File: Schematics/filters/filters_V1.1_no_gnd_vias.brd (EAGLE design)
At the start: 100.6 x 47.9 mm, 110 parts, among them IC1 NE5532N, IC2 NE5532N, IC3 NE5532N, IC4 NE5532N, IC5 NE5532N, IC6 NE5532N, IC7 NE5532N, J1 3_PIN_AMPCONN, J2 3_PIN_AMPCONN, J3 3_PIN_AMPCONN

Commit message: newest gerbers
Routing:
- net N$5: vias 1 -> 0
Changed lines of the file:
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@@
 <wire x1="12.7" y1="15.5575" x2="12.7" y2="14.605" width="0.4064" layer="16"/>
 <wire x1="12.7" y1="14.605" x2="14.605" y2="12.7" width="0.4064" layer="16"/>
-<via x="14.605" y="12.7" extent="1-16" drill="0.381"/>
+<wire x1="14.605" y1="12.7" x2="14.605" y2="12.7" width="0" layer="19" extent="1-16"/>
 <wire x1="14.605" y1="12.7" x2="16.8275" y2="10.4775" width="0.4064" layer="1"/>
 <wire x1="16.8275" y1="10.4775" x2="16.8275" y2="8.4826125" width="0.4064" layer="1"/>
@@
 <contactref element="L12" pad="2"/>
 <contactref element="C11" pad="1"/>
-<via x="32.7025" y="30.1625" extent="1-16" drill="0.8128"/>
+<via x="32.7025" y="30.1625" extent="1-16" drill="0.508"/>
 <wire x1="32.7025" y1="30.1625" x2="32.7025" y2="35.56" width="0.4064" layer="1"/>
 <wire x1="35.56" y1="36.195" x2="37.505" y2="36.195" width="0.8128" layer="1"/>
@@
 <contactref element="R29" pad="2"/>
 <contactref element="VR4" pad="1'"/>
-<via x="80.5815" y="5.08" extent="1-16" drill="0.8128"/>
+<via x="80.5815" y="5.08" extent="1-16" drill="0.508"/>
 <wire x1="80.5815" y1="5.08" x2="74.6125" y2="5.08" width="0.4064" layer="16"/>
 <wire x1="74.6125" y1="5.08" x2="73.9775" y2="4.445" width="0.4064" layer="16"/>
@@
 <contactref element="VR3" pad="1'"/>
 <wire x1="58.1025" y1="7.62" x2="58.1025" y2="5.08" width="0.4064" layer="1"/>
-<via x="58.1025" y="5.08" extent="1-16" drill="0.8128"/>
+<via x="58.1025" y="5.08" extent="1-16" drill="0.508"/>
 <wire x1="58.1025" y1="5.08" x2="52.07" y2="5.08" width="0.4064" layer="16"/>
 <wire x1="52.07" y1="5.08" x2="51.435" y2="4.445" width="0.4064" layer="16"/>
@@
 <contactref element="VR2" pad="1'"/>
 <wire x1="35.56" y1="6.985" x2="35.56" y2="5.3975" width="0.4064" layer="1"/>
-<via x="35.56" y="5.3975" extent="1-16" drill="0.8128"/>
+<via x="35.56" y="5.3975" extent="1-16" drill="0.508"/>
 <wire x1="35.56" y1="5.3975" x2="29.21" y2="5.3975" width="0.4064" layer="16"/>
 <wire x1="29.21" y1="5.3975" x2="28.575" y2="4.7625" width="0.4064" layer="16"/>
@@
 <wire x1="96.2025" y1="7.9375" x2="90.805" y2="7.9375" width="0.4064" layer="1"/>
 <wire x1="90.805" y1="7.9375" x2="90.805" y2="10.4775" width="0.4064" layer="1"/>
-<via x="82.804" y="6.985" extent="1-16" drill="0.8128"/>
+<via x="82.804" y="6.985" extent="1-16" drill="0.508"/>
 <wire x1="82.804" y1="6.985" x2="73.9775" y2="6.985" width="0.4064" layer="16"/>
 <wire x1="73.9775" y1="6.985" x2="72.39" y2="8.5725" width="0.4064" layer="16"/>
@@
 <wire x1="86.27411875" y1="3.936628125" x2="86.70560625" y2="3.378140625" width="0.3048" layer="16"/>
 <wire x1="86.70560625" y1="3.378140625" x2="86.70560625" y2="1.55939375" width="0.3048" layer="16"/>
-<via x="92.867840625" y="1.79724375" extent="1-16" drill="0.8128"/>
+<via x="92.867840625" y="1.79724375" extent="1-16" drill="0.508"/>
 <wire x1="92.867840625" y1="1.79724375" x2="92.867840625" y2="2.8362375" width="0.4064" layer="1"/>
 <wire x1="92.867840625" y1="2.8362375" x2="92.381596875" y2="3.32248125" width="0.4064" layer="1"/>
@@
 <wire x1="86.919915625" y1="1.375271875" x2="85.59364375" y2="1.375271875" width="0.4064" layer="1"/>
 <wire x1="85.59364375" y1="1.375271875" x2="85.5774625" y2="1.391453125" width="0.4064" layer="1"/>
-<via x="85.5774625" y="1.391453125" extent="1-16" drill="0.8128"/>
+<via x="85.5774625" y="1.391453125" extent="1-16" drill="0.508"/>
 <wire x1="85.5774625" y1="1.391453125" x2="82.973725" y2="1.391453125" width="0.4064" layer="16"/>
 <wire x1="82.973725" y1="1.391453125" x2="82.08384375" y2="2.281334375" width="0.4064" layer="16"/>
@@
 <wire x1="86.36" y1="13.335" x2="86.995" y2="12.7" width="0.4064" layer="1"/>
 <wire x1="86.995" y1="12.7" x2="91.44" y2="12.7" width="0.4064" layer="1"/>
-<via x="91.44" y="12.7" extent="1-16" drill="0.8128"/>
+<via x="91.44" y="12.7" extent="1-16" drill="0.508"/>
 <wire x1="91.44" y1="12.7" x2="91.44" y2="11.43" width="0.4064" layer="16"/>
 <wire x1="91.44" y1="11.43" x2="89.535" y2="9.525" width="0.4064" layer="16"/>

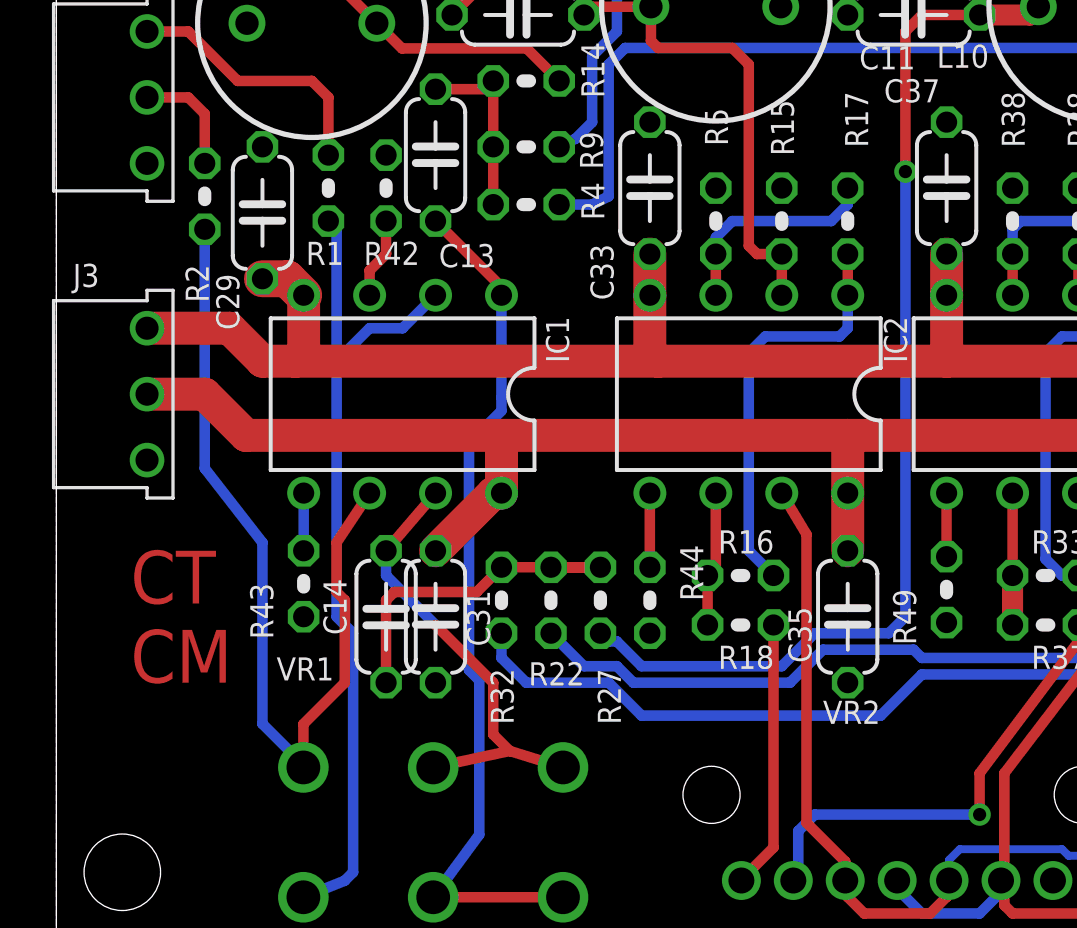
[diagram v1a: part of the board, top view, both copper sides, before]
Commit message: PCB updated and fixed stupid backwards opamps.
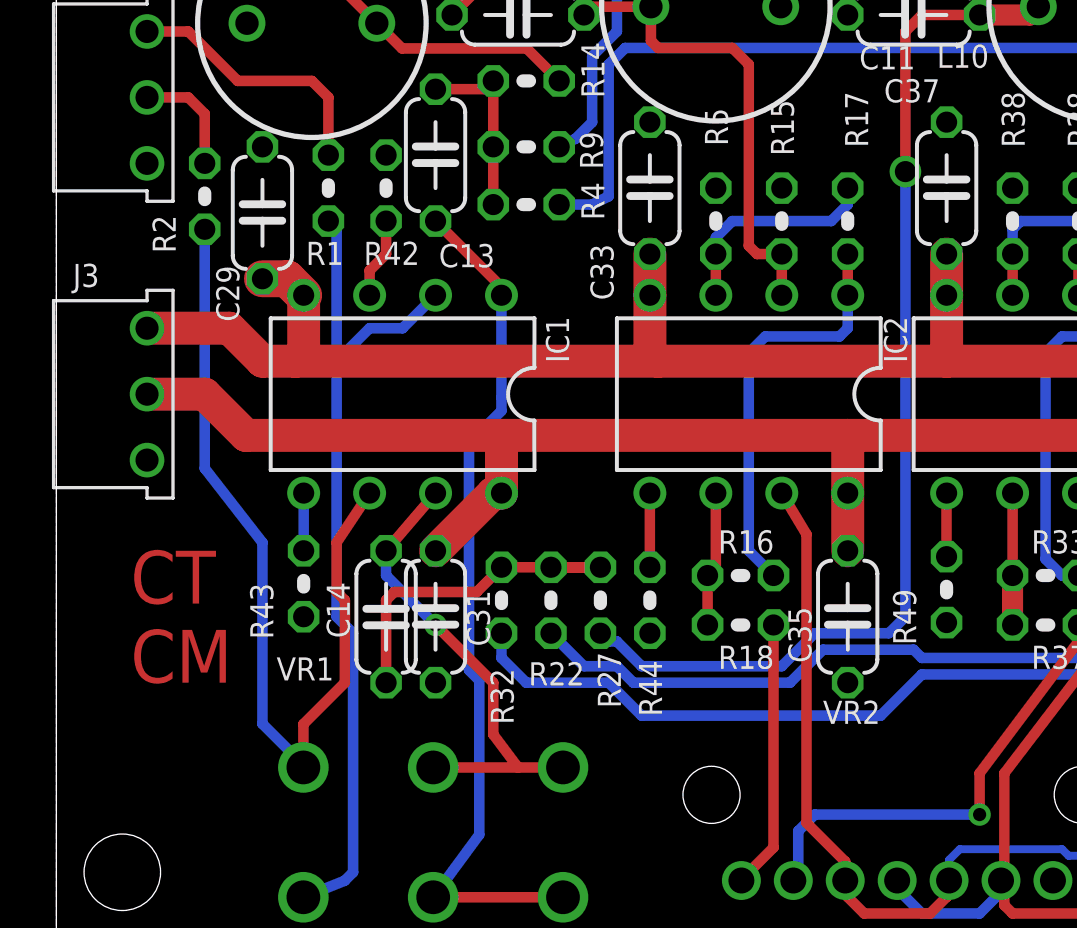
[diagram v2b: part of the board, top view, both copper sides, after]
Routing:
- net N$5: track 17.8 -> 18.3 mm, vias 0 -> 1
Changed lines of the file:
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@@
 </element>
 <element name="C14" library="rcl" package="C050-024X044" value="47u" x="12.7" y="13.0175" smashed="yes" rot="R270">
-<attribute name="NAME" x="10.287" y="14.478" size="0.889" layer="25" font="vector" ratio="15" rot="R270"/>
+<attribute name="NAME" x="11.303" y="12.192" size="0.889" layer="25" font="vector" ratio="15" rot="R90"/>
 <attribute name="VALUE" x="10.033" y="14.7955" size="1.27" layer="27" ratio="10" rot="R270"/>
 </element>
@@
 </element>
 <element name="C29" library="rcl" package="C050-024X044" value="0.1uF" x="7.9375" y="28.575" smashed="yes" rot="R90">
-<attribute name="NAME" x="6.1595" y="26.2255" size="0.889" layer="25" font="vector" ratio="15" rot="R270"/>
+<attribute name="NAME" x="6.1595" y="26.543" size="0.889" layer="25" font="vector" ratio="15" rot="R270"/>
 <attribute name="VALUE" x="10.6045" y="26.797" size="1.27" layer="27" ratio="10" rot="R90"/>
 </element>
@@
 </element>
 <element name="R27" library="rcl" package="0204V" value="50" x="20.955" y="13.6525" smashed="yes" rot="R270">
-<attribute name="NAME" x="20.8534" y="11.0236" size="0.889" layer="25" font="vector" ratio="15" rot="R270"/>
+<attribute name="NAME" x="20.8534" y="11.6586" size="0.889" layer="25" font="vector" ratio="15" rot="R270"/>
 <attribute name="VALUE" x="18.6436" y="15.7861" size="1.27" layer="27" ratio="10" rot="R270"/>
 </element>
@@
 </element>
 <element name="R2" library="rcl" package="0204V" value="10k" x="5.715" y="29.21" smashed="yes" rot="R270">
-<attribute name="NAME" x="4.9784" y="26.5811" size="0.889" layer="25" font="vector" ratio="15" rot="R270"/>
+<attribute name="NAME" x="3.7084" y="28.4861" size="0.889" layer="25" font="vector" ratio="15" rot="R270"/>
 <attribute name="VALUE" x="3.4036" y="31.3436" size="1.27" layer="27" ratio="10" rot="R270"/>
 </element>
@@
 </element>
 <element name="R44" library="rcl" package="0204V" value="4.7k" x="22.86" y="13.6525" smashed="yes" rot="R270">
-<attribute name="NAME" x="24.0284" y="15.7861" size="0.889" layer="25" font="vector" ratio="15" rot="R270"/>
+<attribute name="NAME" x="22.4409" y="11.3411" size="0.889" layer="25" font="vector" ratio="15" rot="R270"/>
 <attribute name="VALUE" x="20.5486" y="15.7861" size="1.27" layer="27" ratio="10" rot="R270"/>
 </element>
@@
 <contactref element="VR1" pad="3'"/>
 <contactref element="VR1" pad="2'"/>
-<wire x1="14.5139625" y1="7.2126125" x2="17.4625" y2="7.8476125" width="0.4064" layer="1"/>
+<wire x1="14.5139625" y1="7.2126125" x2="17.78" y2="7.2126125" width="0.4064" layer="1"/>
 <contactref element="IC1" pad="7"/>
-<wire x1="17.4625" y1="7.8476125" x2="19.5139625" y2="7.2126125" width="0.4064" layer="1"/>
+<wire x1="17.78" y1="7.2126125" x2="19.5139625" y2="7.2126125" width="0.4064" layer="1"/>
 <wire x1="14.605" y1="17.78" x2="12.7" y2="15.5575" width="0.4064" layer="1"/>
 <wire x1="12.7" y1="15.5575" x2="12.7" y2="14.605" width="0.4064" layer="16"/>
 <wire x1="12.7" y1="14.605" x2="14.605" y2="12.7" width="0.4064" layer="16"/>
-<wire x1="14.605" y1="12.7" x2="14.605" y2="12.7" width="0" layer="19" extent="1-16"/>
 <wire x1="14.605" y1="12.7" x2="16.8275" y2="10.4775" width="0.4064" layer="1"/>
 <wire x1="16.8275" y1="10.4775" x2="16.8275" y2="8.4826125" width="0.4064" layer="1"/>
-<wire x1="16.8275" y1="8.4826125" x2="17.4625" y2="7.8476125" width="0.4064" layer="1"/>
+<wire x1="16.8275" y1="8.4826125" x2="17.78" y2="7.2126125" width="0.4064" layer="1"/>
+<via x="14.605" y="12.7" extent="1-16" drill="0.508"/>
 </signal>
 <signal name="N$14">
@@
 <contactref element="L12" pad="2"/>
 <contactref element="C11" pad="1"/>
-<via x="32.7025" y="30.1625" extent="1-16" drill="0.508"/>
+<via x="32.7025" y="30.1625" extent="1-16" drill="0.8128"/>
 <wire x1="32.7025" y1="30.1625" x2="32.7025" y2="35.56" width="0.4064" layer="1"/>
 <wire x1="35.56" y1="36.195" x2="37.505" y2="36.195" width="0.8128" layer="1"/>
